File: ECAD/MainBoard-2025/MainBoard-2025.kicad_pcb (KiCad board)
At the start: 2 copper layers, 100 x 100 mm, 147 parts, among them J1 XT60, J10 Conn_01x02, J11 Conn_01x03, J12 Conn_01x04, J13 Conn_01x03, J14 Conn_01x03, J15 Conn_01x02, J16 XT30, J17 XT30, J18 Conn_01x02, J2 Conn_01x04, J20 BAU, J21 BAU, J22 Conn_01x04, J23 Conn_01x02, J26 BAU, J27 BAU, J28 Conn_01x02, J29 Conn_01x02, J3 ConStep1, J4 Conn_01x02, J5 ConStep1, J6 ConStep1, J7 XT30, J8 Conn_01x02, J9 Conn_01x02, K2 FINDER-36.11, U1 Teensy3.5_All_Pins, U2 R-78B3.3-2.0, U3 R-78B12-2.0, U4 R-78B5.0-2.0, U5 Teensy4.1

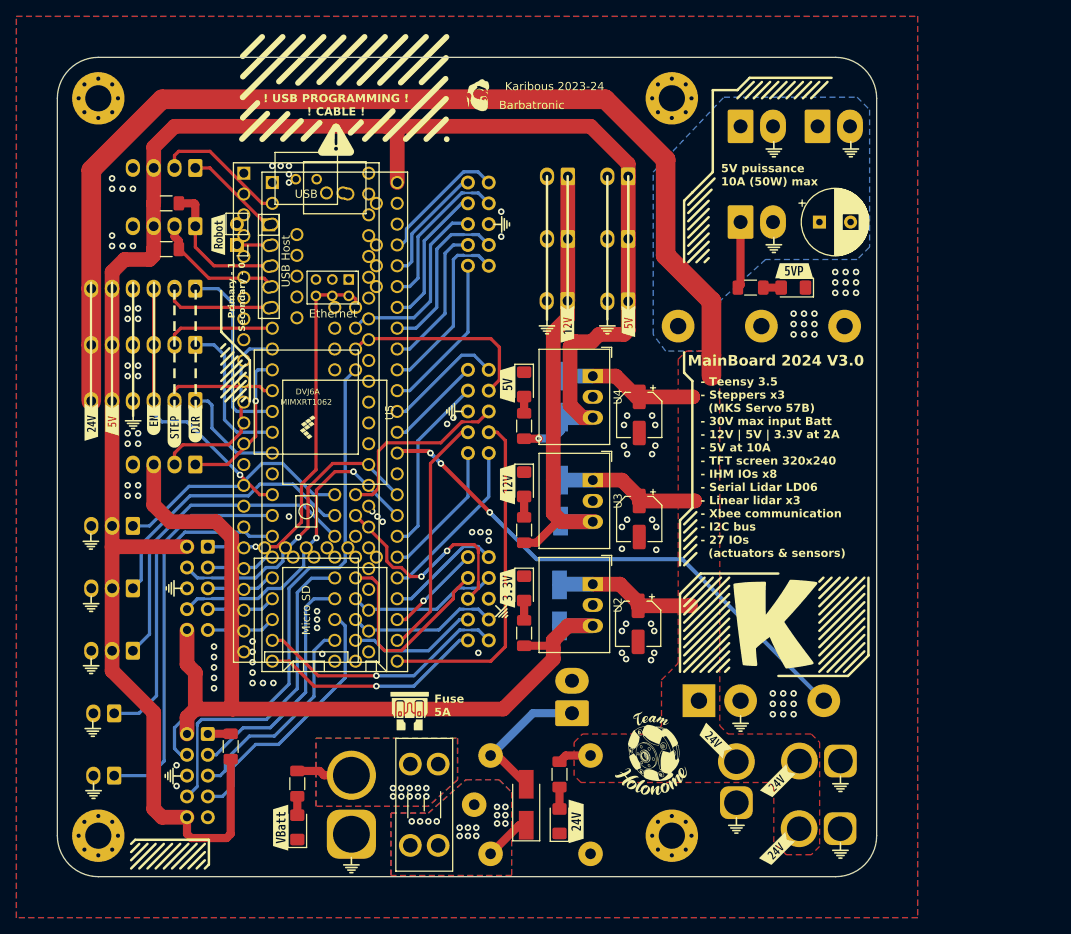
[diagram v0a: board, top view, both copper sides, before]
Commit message: add buzzer and res on program
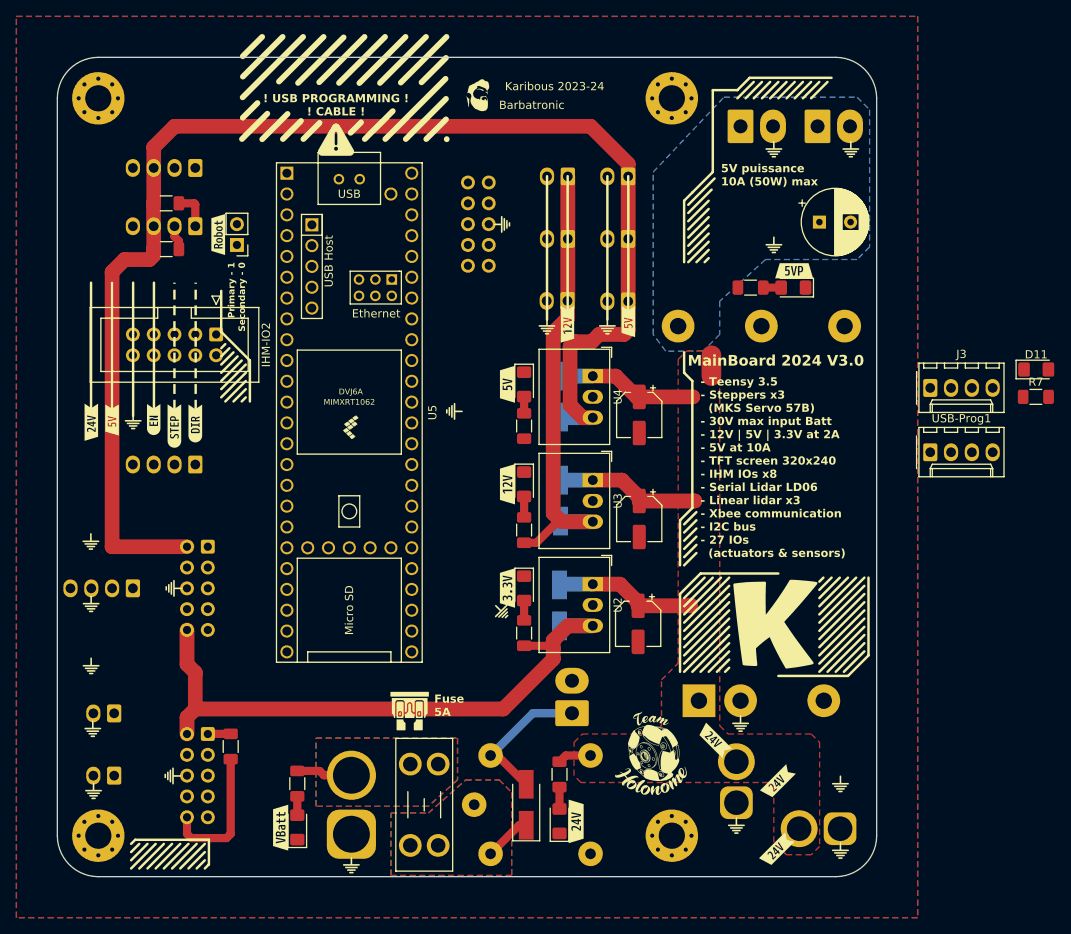
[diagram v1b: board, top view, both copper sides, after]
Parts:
- removed C_Act2, C_Act3: Conn_02x05_Odd_Even, Connector_IDC:IDC-Header_2x05_P2.54mm_Vertical
- removed J13, J14: Conn_01x03, Connector_Molex:Molex_KK-254_AE-6410-03A_1x03_P2.54mm_Vertical
- removed J17: XT30, Connector_AMASS:AMASS_XT30U-F_1x02_P5.0mm_Vertical
- removed J27: BAU, Connector_Molex:Molex_KK-396_A-41791-0002_1x02_P3.96mm_Vertical
- removed J5, J6: ConStep1, Connector_Molex:Molex_KK-254_AE-6410-06A_1x06_P2.54mm_Vertical
- removed U1: Teensy3.5_All_Pins, Teensy:Teensy35_36_All_Pins
- added D11: LED_Small, LED_SMD:LED_1206_3216Metric_Pad1.42x1.75mm_HandSolder, F.Cu at (219.5, 88.1)
- added IHM-IO2: Conn_02x05_Odd_Even, Connector_IDC:IDC-Header_2x05_P2.54mm_Vertical, F.Cu at (119.4, 83.8)
- added R7: R_Small, Resistor_SMD:R_1206_3216Metric_Pad1.30x1.75mm_HandSolder, F.Cu at (219.4, 91.4)
- added USB-Prog1: Conn_01x04, Connector_Molex:Molex_KK-254_AE-6410-04A_1x04_P2.54mm_Vertical, F.Cu at (206.5, 98.2)
- J11: value Conn_01x03 -> Conn_01x04; footprint Connector_Molex:Molex_KK-254_AE-6410-03A_1x03_P2.54mm_Vertical -> Connector_Molex:Molex_KK-254_AE-6410-04A_1x04_P2.54mm_Vertical
- J3: value ConStep1 -> Conn_01x04; footprint Connector_Molex:Molex_KK-254_AE-6410-06A_1x06_P2.54mm_Vertical -> Connector_Molex:Molex_KK-254_AE-6410-04A_1x04_P2.54mm_Vertical; moved to F.Cu
- moved J3 89.9 mm to (206.5, 90.3), turned to 0 degrees
- moved U5 5.26 mm to (135.6, 93.3)
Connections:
- IHM-IO1 pad 4: DAC1 -> Analog1
- IHM-IO1 pad 8: DAC0 -> Analog0
- J11 pad 1: Sensor-02 -> D+ Host
- J11 pad 2: +5V -> D- Host
- J11 pad 3: GND -> +5V
- J3 pad 1: DIR_2 -> RX-loc
- J3 pad 2: STEP_2 -> TX-loc
- J3 pad 3: EN -> +5V
- U5 pad 11: STEP_3 -> TFT_DC
- U5 pad 12: DIR_1 -> TFT_CS
- U5 pad 13: DIR_2 -> TFT_MOSI
- U5 pad 14: DIR_3 -> TFT_MISO
- U5 pad 17: Init -> DIR_1
- U5 pad 18: Tirette -> DIR_2
- U5 pad 19: Couleur -> DIR_3
- U5 pad 20: Detection -> En5VP
- U5 pad 21: IHM_3 -> Init
- U5 pad 22: IHM_4 -> Tirette
- U5 pad 23: C_Act3-2 -> Couleur
- U5 pad 24: C_Act3-1 -> Detection
- U5 pad 25: C_Act2-4 -> IHM_3
- U5 pad 26: C_Act2-3 -> TX-loc
- U5 pad 27: C_Act3-7 -> RX-loc
- U5 pad 28: C_Act3-8 -> IHM_4
- U5 pad 29: C_Act2-2 -> NEO_PIXEL
- U5 pad 30: C_Act2-1 -> Analog0
- U5 pad 31: C_Act2-5 -> Analog1
- U5 pad 33: unconnected-(U5-41_A17-Pad33) -> C_Act1-6
- U5 pad 35: En5VP -> TFT_SCK
- U5 pad 36: C_Act2-7 -> C_Act1-8
- U5 pad 37: C_Act2-8 -> C_Act1-7
- U5 pad 38: C_Act1-1 -> C_Act1-5
- U5 pad 39: C_Act1-2 -> C_Act1-9
- U5 pad 40: C_Act1-3 -> SDA
- U5 pad 41: C_Act1-4 -> SCL
- U5 pad 42: C_Act1-5 -> C_Act1-3
- U5 pad 43: C_Act1-6 -> C_Act1-1
- U5 pad 44: C_Act1-7 -> C_Act1-2
- U5 pad 45: C_Act1-8 -> C_Act1-4
- U5 pad 5: SCL -> unconnected-(U5-3_LRCLK2-Pad5)
- U5 pad 56: unconnected-(U5-D--Pad56) -> D- Host
- U5 pad 57: unconnected-(U5-D+-Pad57) -> D+ Host
- U5 pad 6: SDA -> STEP_1
- U5 pad 7: STEP_1 -> STEP_2
- U5 pad 8: STEP_2 -> STEP_3
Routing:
- net +24V: track 190.1 -> 58.9 mm
- net En5VP: track 64.8 -> 0.00 mm, vias 3 -> 0
- net TFT_DC: track 64.4 -> 0.00 mm
- net +5V: track 235.5 -> 182.3 mm, vias 1 -> 0
- net NEO_PIXEL: track 46.9 -> 0.00 mm, vias 1 -> 0
- net Tirette: track 46.7 -> 0.00 mm
- net C_Act2-4: track 41.5 -> 0.00 mm
- net TFT_CS: track 40.4 -> 0.00 mm
- net Init: track 39.7 -> 0.00 mm
- net Sensor-01: track 39.7 -> 0.00 mm
- net DAC0: track 39.3 -> 0.00 mm, vias 2 -> 0
- net +3V3: track 112.5 -> 75.4 mm
- net DAC1: track 36.9 -> 0.00 mm, vias 2 -> 0
- net Sensor-02: track 34.0 -> 0.00 mm
- net EN: track 33.8 -> 0.00 mm, vias 1 -> 0
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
